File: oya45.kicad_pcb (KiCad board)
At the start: 2 copper layers, 94 parts, among them U1 ProMicro

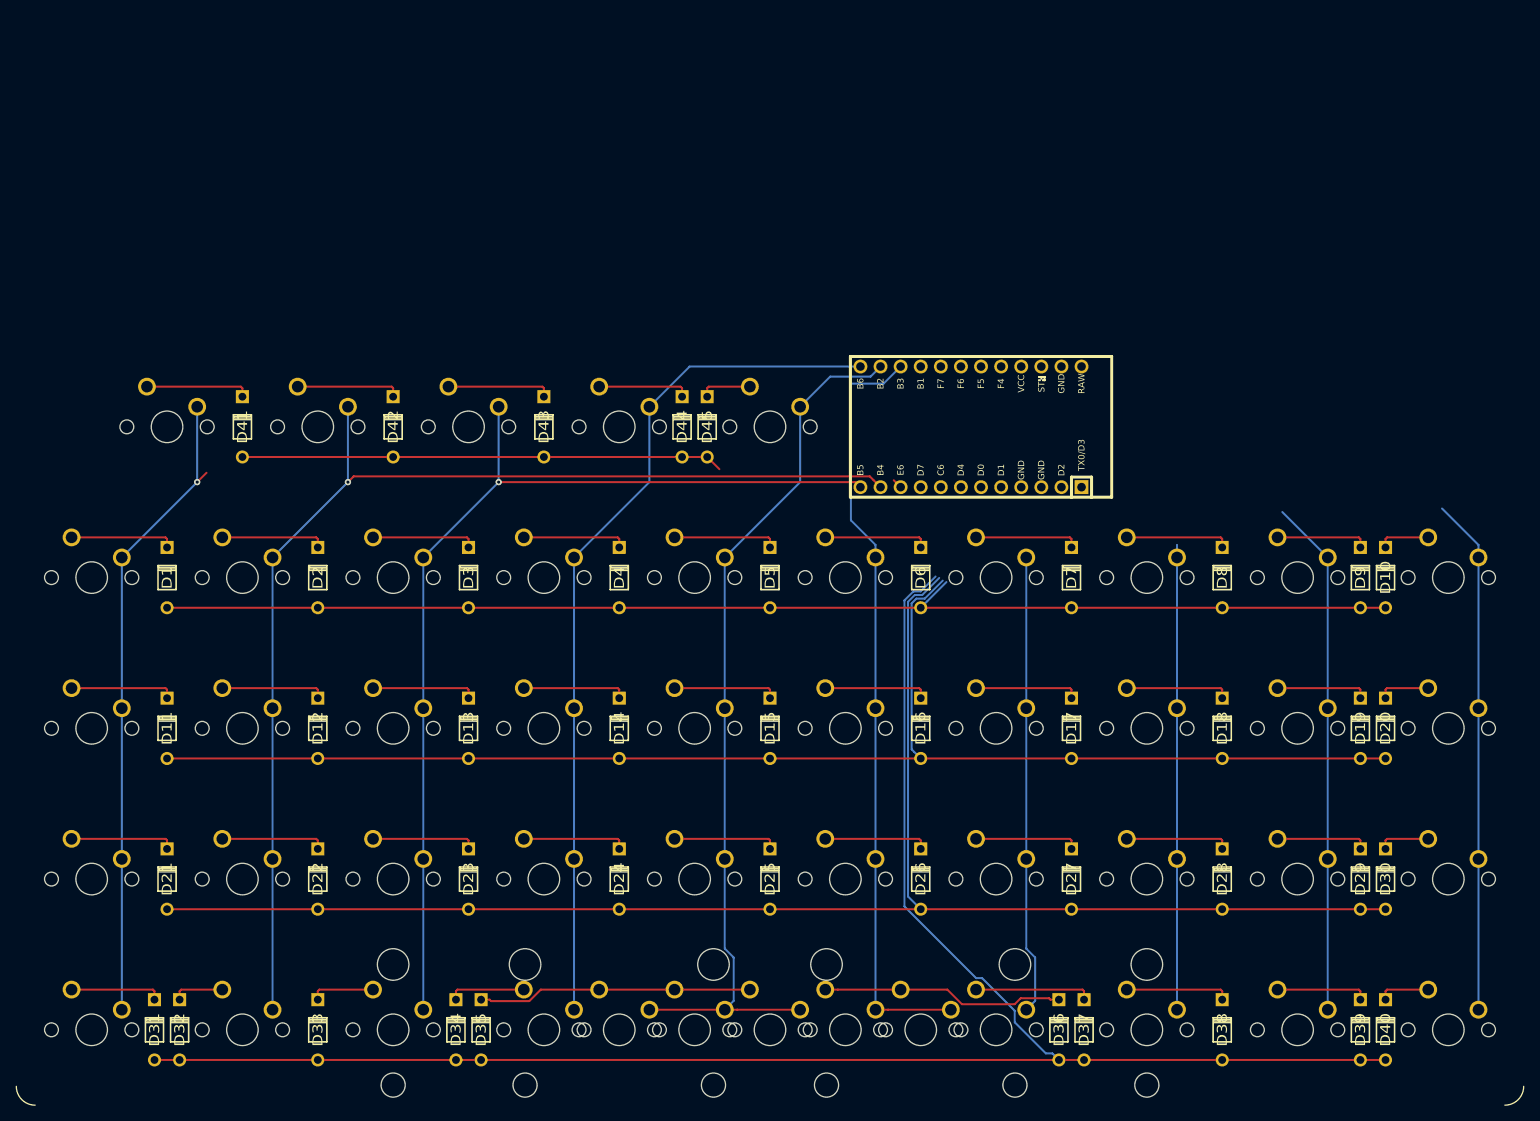
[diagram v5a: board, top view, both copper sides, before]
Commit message: cleaned col and row with first clean routing
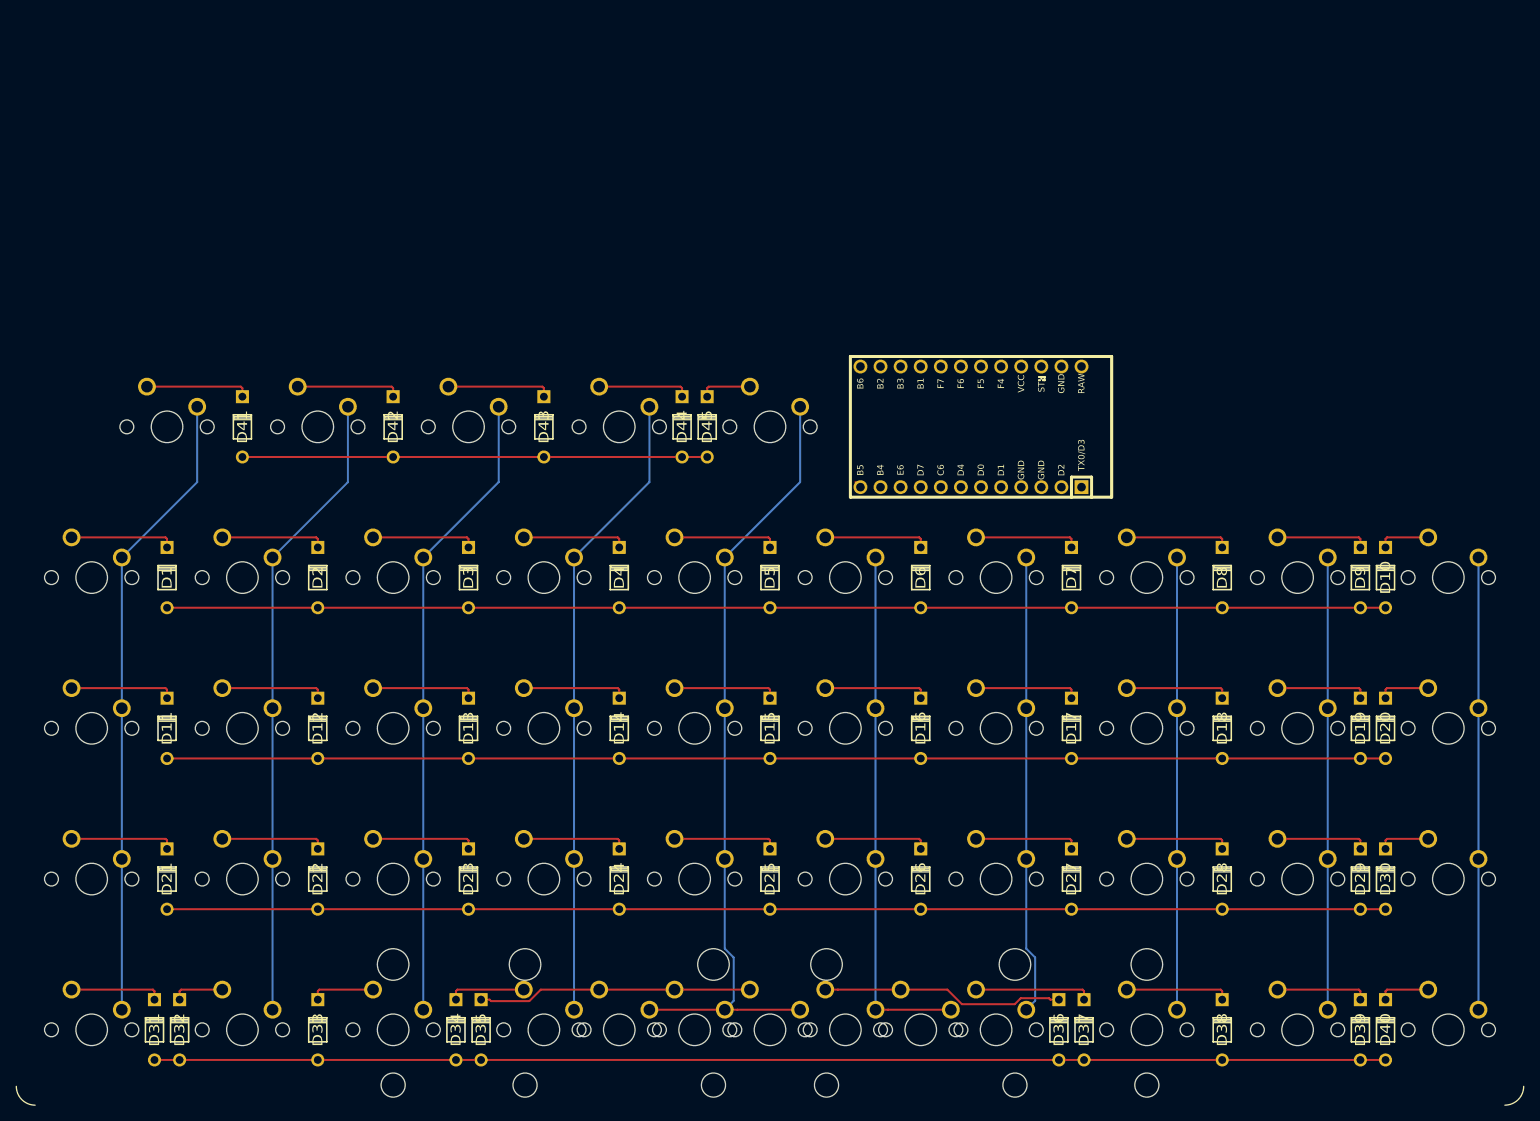
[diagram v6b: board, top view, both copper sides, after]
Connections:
- U1 pad 10: col0 -> row2
- U1 pad 11: col1 -> row1
- U1 pad 12: col2 -> row0
- U1 pad 13: col3 -> col0
- U1 pad 14: col4 -> col1
- U1 pad 15: col5 -> col2
- U1 pad 16: col6 -> col3
- U1 pad 17: col7 -> col4
- U1 pad 18: col8 -> col5
- U1 pad 19: col9 -> col6
- U1 pad 5: row0 -> col9
- U1 pad 6: row1 -> col8
- U1 pad 7: row2 -> col7
- U1 pad 8: row3 -> row4
- U1 pad 9: row4 -> row3
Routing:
- net row4: track 227.9 -> 155.6 mm
- net col1: track 148.3 -> 80.1 mm, vias 1 -> 0
- net col2: track 126.1 -> 80.1 mm, vias 1 -> 0
- net row3: track 198.7 -> 154.0 mm
- net col5: track 97.1 -> 66.7 mm
- net col3: track 108.9 -> 80.1 mm
- net row2: track 179.2 -> 154.0 mm
- net col4: track 112.4 -> 100.1 mm
- net col8: track 65.3 -> 57.2 mm
- net col9: track 65.2 -> 57.2 mm
- net row1: track 158.6 -> 154.0 mm
- net col0: track 83.1 -> 80.1 mm, vias 1 -> 0
- net col7: track 58.7 -> 57.2 mm
- net row0: track 60.9 -> 59.6 mm

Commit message: created gerbers and fixed routing
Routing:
- net col0: track 80.1 -> 166.1 mm
- net row4: track 155.6 -> 234.6 mm
- net col1: track 80.1 -> 150.1 mm
- net col6: track 58.1 -> 126.1 mm
- net col9: track 57.2 -> 121.2 mm
- net row3: track 154.0 -> 209.3 mm
- net col2: track 80.1 -> 133.5 mm
- net col5: track 66.7 -> 115.6 mm
- net col8: track 57.2 -> 104.6 mm
- net row2: track 154.0 -> 190.7 mm
- net col3: track 80.1 -> 116.5 mm
- net col7: track 57.2 -> 88.1 mm
- net col4: track 100.1 -> 124.7 mm
- net row0: track 59.6 -> 80.6 mm
- net row1: track 154.0 -> 172.3 mm
